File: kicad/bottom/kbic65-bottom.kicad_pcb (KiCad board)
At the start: 2 copper layers, 314.3 x 138.9 mm, 16 parts

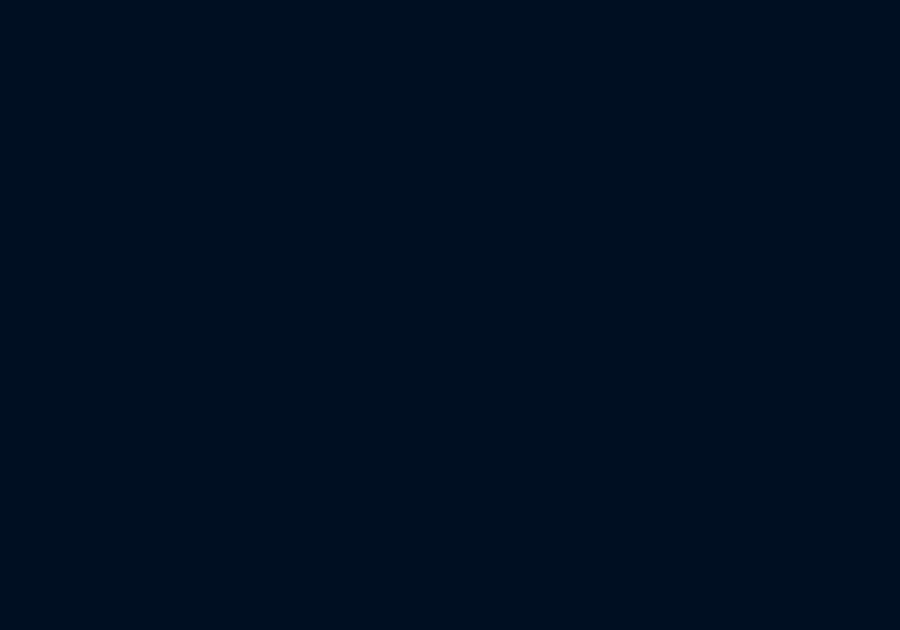
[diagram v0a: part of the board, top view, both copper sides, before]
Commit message: added ref placeholders and created gerbers
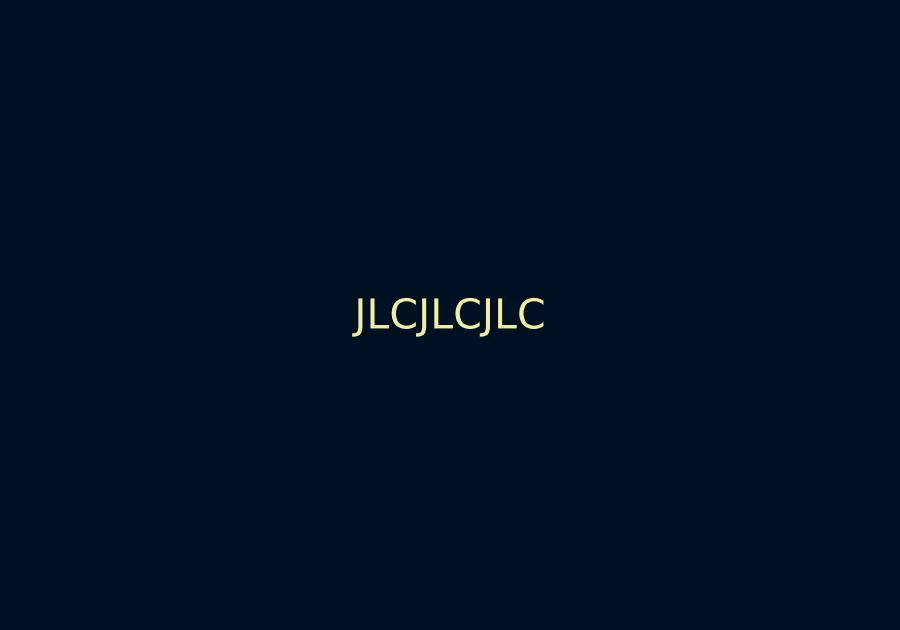
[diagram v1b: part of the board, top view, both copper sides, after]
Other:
- board text added: "JLCJLCJLC"
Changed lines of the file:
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@@
   (general
     (thickness 1.6)
-    (drawings 347)
+    (drawings 348)
     (tracks 0)
     (zones 0)
@@
     (visible_elements 7FFFEFFF)
     (pcbplotparams
-      (layerselection 0x010fc_ffffffff)
+      (layerselection 0x010f0_ffffffff)
       (usegerberextensions false)
       (usegerberattributes true)
@@
       (outputformat 1)
       (mirror false)
-      (drillshape 1)
+      (drillshape 0)
       (scaleselection 1)
-      (outputdirectory ""))
+      (outputdirectory "gerber"))
   )
   (net 0 "")
@@
       (effects (font (size 1 1) (thickness 0.15)))
     )
-    (fp_circle (center 0 0) (end 2.45 0) (layer F.CrtYd) (width 0.05))
-    (fp_circle (center 0 0) (end 2.2 0) (layer Cmts.User) (width 0.15))
+    (fp_circle (center 0 0) (end 2.2 0) (layer Cmts.User) (width 0.15))
+    (fp_circle (center 0 0) (end 2.45 0) (layer F.CrtYd) (width 0.05))
     (fp_text user %R (at 0.3 0) (layer F.Fab)
       (effects (font (size 1 1) (thickness 0.15)))
@@
       (effects (font (size 1 1) (thickness 0.15)))
     )
-    (fp_circle (center 0 0) (end 2.45 0) (layer F.CrtYd) (width 0.05))
-    (fp_circle (center 0 0) (end 2.2 0) (layer Cmts.User) (width 0.15))
+    (fp_circle (center 0 0) (end 2.2 0) (layer Cmts.User) (width 0.15))
+    (fp_circle (center 0 0) (end 2.45 0) (layer F.CrtYd) (width 0.05))
     (fp_text user %R (at 0.3 0) (layer F.Fab)
       (effects (font (size 1 1) (thickness 0.15)))
@@
       (effects (font (size 1 1) (thickness 0.15)))
     )
-    (fp_circle (center 0 0) (end 2.45 0) (layer F.CrtYd) (width 0.05))
-    (fp_circle (center 0 0) (end 2.2 0) (layer Cmts.User) (width 0.15))
+    (fp_circle (center 0 0) (end 2.2 0) (layer Cmts.User) (width 0.15))
+    (fp_circle (center 0 0) (end 2.45 0) (layer F.CrtYd) (width 0.05))
     (fp_text user %R (at 0.3 0) (layer F.Fab)
       (effects (font (size 1 1) (thickness 0.15)))
@@
       (effects (font (size 1 1) (thickness 0.15)))
     )
-    (fp_circle (center 0 0) (end 2.45 0) (layer F.CrtYd) (width 0.05))
-    (fp_circle (center 0 0) (end 2.2 0) (layer Cmts.User) (width 0.15))
+    (fp_circle (center 0 0) (end 2.2 0) (layer Cmts.User) (width 0.15))
+    (fp_circle (center 0 0) (end 2.45 0) (layer F.CrtYd) (width 0.05))
     (fp_text user %R (at 0.3 0) (layer F.Fab)
       (effects (font (size 1 1) (thickness 0.15)))
@@
       (effects (font (size 1 1) (thickness 0.15)))
     )
-    (fp_circle (center 0 0) (end 2.45 0) (layer F.CrtYd) (width 0.05))
-    (fp_circle (center 0 0) (end 2.2 0) (layer Cmts.User) (width 0.15))
+    (fp_circle (center 0 0) (end 2.2 0) (layer Cmts.User) (width 0.15))
+    (fp_circle (center 0 0) (end 2.45 0) (layer F.CrtYd) (width 0.05))
     (fp_text user %R (at 0.3 0) (layer F.Fab)
       (effects (font (size 1 1) (thickness 0.15)))
@@
       (effects (font (size 1 1) (thickness 0.15)))
     )
-    (fp_circle (center 0 0) (end 2.45 0) (layer F.CrtYd) (width 0.05))
-    (fp_circle (center 0 0) (end 2.2 0) (layer Cmts.User) (width 0.15))
+    (fp_circle (center 0 0) (end 2.2 0) (layer Cmts.User) (width 0.15))
+    (fp_circle (center 0 0) (end 2.45 0) (layer F.CrtYd) (width 0.05))
     (fp_text user %R (at 0.3 0) (layer F.Fab)
       (effects (font (size 1 1) (thickness 0.15)))
@@
       (effects (font (size 1 1) (thickness 0.15)))
     )
-    (fp_circle (center 0 0) (end 2.45 0) (layer F.CrtYd) (width 0.05))
-    (fp_circle (center 0 0) (end 2.2 0) (layer Cmts.User) (width 0.15))
+    (fp_circle (center 0 0) (end 2.2 0) (layer Cmts.User) (width 0.15))
+    (fp_circle (center 0 0) (end 2.45 0) (layer F.CrtYd) (width 0.05))
     (fp_text user %R (at 0.3 0) (layer F.Fab)
       (effects (font (size 1 1) (thickness 0.15)))
@@
       (effects (font (size 1 1) (thickness 0.15)))
     )
-    (fp_circle (center 0 0) (end 2.45 0) (layer F.CrtYd) (width 0.05))
-    (fp_circle (center 0 0) (end 2.2 0) (layer Cmts.User) (width 0.15))
+    (fp_circle (center 0 0) (end 2.2 0) (layer Cmts.User) (width 0.15))
+    (fp_circle (center 0 0) (end 2.45 0) (layer F.CrtYd) (width 0.05))
     (fp_text user %R (at 0.3 0) (layer F.Fab)
       (effects (font (size 1 1) (thickness 0.15)))
@@
       (effects (font (size 1 1) (thickness 0.15)))
     )
-    (fp_circle (center 0 0) (end 2.45 0) (layer F.CrtYd) (width 0.05))
-    (fp_circle (center 0 0) (end 2.2 0) (layer Cmts.User) (width 0.15))
+    (fp_circle (center 0 0) (end 2.2 0) (layer Cmts.User) (width 0.15))
+    (fp_circle (center 0 0) (end 2.45 0) (layer F.CrtYd) (width 0.05))
     (fp_text user %R (at 0.3 0) (layer F.Fab)
       (effects (font (size 1 1) (thickness 0.15)))
@@
       (effects (font (size 1 1) (thickness 0.15)))
     )
-    (fp_circle (center 0 0) (end 2.45 0) (layer F.CrtYd) (width 0.05))
-    (fp_circle (center 0 0) (end 2.2 0) (layer Cmts.User) (width 0.15))
+    (fp_circle (center 0 0) (end 2.2 0) (layer Cmts.User) (width 0.15))
+    (fp_circle (center 0 0) (end 2.45 0) (layer F.CrtYd) (width 0.05))
     (fp_text user %R (at 0.3 0) (layer F.Fab)
       (effects (font (size 1 1) (thickness 0.15)))
@@
       (effects (font (size 1 1) (thickness 0.15)))
     )
-    (fp_circle (center 0 0) (end 2.45 0) (layer F.CrtYd) (width 0.05))
-    (fp_circle (center 0 0) (end 2.2 0) (layer Cmts.User) (width 0.15))
+    (fp_circle (center 0 0) (end 2.2 0) (layer Cmts.User) (width 0.15))
+    (fp_circle (center 0 0) (end 2.45 0) (layer F.CrtYd) (width 0.05))
     (fp_text user %R (at 0.3 0) (layer F.Fab)
       (effects (font (size 1 1) (thickness 0.15)))
@@
       (effects (font (size 1 1) (thickness 0.15)))
     )
-    (fp_circle (center 0 0) (end 2.45 0) (layer F.CrtYd) (width 0.05))
-    (fp_circle (center 0 0) (end 2.2 0) (layer Cmts.User) (width 0.15))
+    (fp_circle (center 0 0) (end 2.2 0) (layer Cmts.User) (width 0.15))
+    (fp_circle (center 0 0) (end 2.45 0) (layer F.CrtYd) (width 0.05))
     (fp_text user %R (at 0.3 0) (layer F.Fab)
       (effects (font (size 1 1) (thickness 0.15)))
@@
       (effects (font (size 1 1) (thickness 0.15)))
     )
-    (fp_circle (center 0 0) (end 2.45 0) (layer F.CrtYd) (width 0.05))
-    (fp_circle (center 0 0) (end 2.2 0) (layer Cmts.User) (width 0.15))
+    (fp_circle (center 0 0) (end 2.2 0) (layer Cmts.User) (width 0.15))
+    (fp_circle (center 0 0) (end 2.45 0) (layer F.CrtYd) (width 0.05))
     (fp_text user %R (at 0.3 0) (layer F.Fab)
       (effects (font (size 1 1) (thickness 0.15)))
@@
       (effects (font (size 1 1) (thickness 0.15)))
     )
-    (fp_circle (center 0 0) (end 2.45 0) (layer F.CrtYd) (width 0.05))
-    (fp_circle (center 0 0) (end 2.2 0) (layer Cmts.User) (width 0.15))
+    (fp_circle (center 0 0) (end 2.2 0) (layer Cmts.User) (width 0.15))
+    (fp_circle (center 0 0) (end 2.45 0) (layer F.CrtYd) (width 0.05))
     (fp_text user %R (at 0.3 0) (layer F.Fab)
       (effects (font (size 1 1) (thickness 0.15)))
@@
       (effects (font (size 1 1) (thickness 0.15)))
     )
-    (fp_circle (center 0 0) (end 2.45 0) (layer F.CrtYd) (width 0.05))
-    (fp_circle (center 0 0) (end 2.2 0) (layer Cmts.User) (width 0.15))
+    (fp_circle (center 0 0) (end 2.2 0) (layer Cmts.User) (width 0.15))
+    (fp_circle (center 0 0) (end 2.45 0) (layer F.CrtYd) (width 0.05))
     (fp_text user %R (at 0.3 0) (layer F.Fab)
       (effects (font (size 1 1) (thickness 0.15)))
@@
       (effects (font (size 1 1) (thickness 0.15)))
     )
-    (fp_circle (center 0 0) (end 2.45 0) (layer F.CrtYd) (width 0.05))
-    (fp_circle (center 0 0) (end 2.2 0) (layer Cmts.User) (width 0.15))
-    (fp_text user %R (at 0.3 0) (layer F.Fab)
-      (effects (font (size 1 1) (thickness 0.15)))
-    )
-    (pad 1 thru_hole circle (at 0 0) (size 4.4 4.4) (drill 2.2) (layers *.Cu *.Mask))
+    (fp_circle (center 0 0) (end 2.2 0) (layer Cmts.User) (width 0.15))
+    (fp_circle (center 0 0) (end 2.45 0) (layer F.CrtYd) (width 0.05))
+    (fp_text user %R (at 0.3 0) (layer F.Fab)
+      (effects (font (size 1 1) (thickness 0.15)))
+    )
+    (pad 1 thru_hole circle (at 0 0) (size 4.4 4.4) (drill 2.2) (layers *.Cu *.Mask))
+  )
+  (gr_text JLCJLCJLC (at 39.6875 -27.78125) (layer F.SilkS)
+    (effects (font (size 1 1) (thickness 0.15)))
   )
   (gr_line (start 69.05625 -113.01875) (end 69.05625 -113.01875) (layer Cmts.User) (width 0.2))

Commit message: added swanky sun (imho)
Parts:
- removed the REF** at (69.1, -111.9)
- removed the REF** at (171.4, -125.4)
- removed the REF** at (171.4, -111.9)
- removed the REF** at (273.8, -111.9)
- added G***: LOGO, sun:sun_600px_169dpi_ditherlicious_mid_exposure, F.Cu at (171.4, -81.0)
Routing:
- added copper zone on F.Cu, net (none)
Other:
- board text added: "JLCJLCJLCJLC"
- board text removed: "JLCJLCJLC"
